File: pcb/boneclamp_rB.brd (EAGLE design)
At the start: 160 x 100 mm, 73 parts, among them IC1 24C, U1 AD8032ARZ-REEL7, U2 LT1964ES5-5TRMPBF, U4 TLV70245DBVT, U7 AD7682BCPZ, U8 TPS63700DRCT, U9 ADA4841-2YRZ

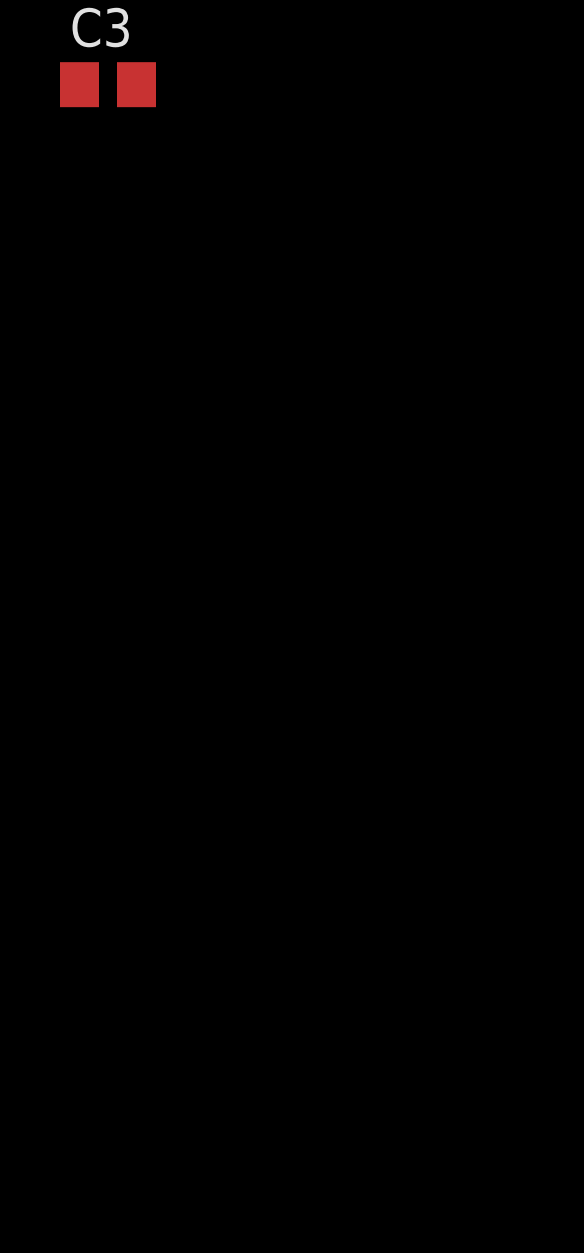
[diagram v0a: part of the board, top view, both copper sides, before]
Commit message: Properly bypassed the power and logic supplies for the DAC
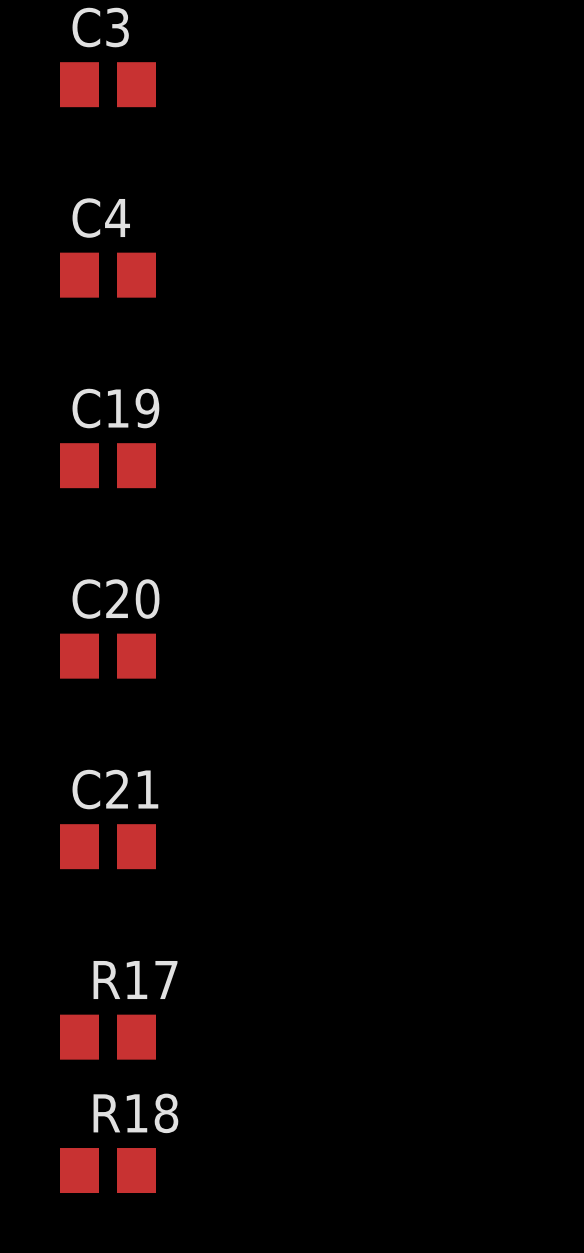
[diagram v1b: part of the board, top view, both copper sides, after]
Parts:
- added C19, C21, C4: 0.1uF, rcl:C0805
- added C20: 10uF, rcl:C0805
- added R17, R18: 10k, rcl:R0805
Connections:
- new net DAC_LDAC: R18.1, U$42.9
- new net PE: C4.2
- net AGND: now also C19.2, C20.2, C21.2; no longer U$42.9
- net DAC_RST: now also R17.1
- net VDD: now also C19.1, C20.1
- net VDRIVE: now also C4.1, R17.2, R18.2
- net VREF: now also C21.1
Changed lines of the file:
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@@
 </element>
 <element name="C3" library="rcl" package="C0805" value="10uF" x="-119.38" y="-366.395"/>
+<element name="C4" library="rcl" package="C0805" value="0.1uF" x="-119.38" y="-372.745"/>
+<element name="C19" library="rcl" package="C0805" value="0.1uF" x="-119.38" y="-379.095"/>
+<element name="C20" library="rcl" package="C0805" value="10uF" x="-119.38" y="-385.445"/>
+<element name="C21" library="rcl" package="C0805" value="0.1uF" x="-119.38" y="-391.795"/>
+<element name="R17" library="rcl" package="R0805" value="10k" x="-119.38" y="-398.145"/>
+<element name="R18" library="rcl" package="R0805" value="10k" x="-119.38" y="-402.59"/>
 </elements>
 <signals>
@@
 </polygon>
 <contactref element="C3" pad="1"/>
+<contactref element="C20" pad="1"/>
+<contactref element="C19" pad="1"/>
+<wire x1="-120.33" y1="-379.095" x2="-120.33" y2="-385.445" width="0" layer="19" extent="1-1"/>
+<wire x1="-120.33" y1="-366.395" x2="-120.33" y2="-379.095" width="0" layer="19" extent="1-1"/>
 <wire x1="-120.33" y1="-355.6" x2="-120.33" y2="-366.395" width="0" layer="19" extent="1-1"/>
 <wire x1="-108.0262" y1="-302.895" x2="-120.33" y2="-355.6" width="0" layer="19" extent="1-1"/>
@@
 <contactref element="U$42" pad="4"/>
 <contactref element="U$42" pad="10"/>
-<contactref element="U$42" pad="9"/>
 <contactref element="U$42" pad="16"/>
 <contactref element="C2" pad="2"/>
@@
 </polygon>
 <contactref element="C3" pad="2"/>
+<contactref element="C20" pad="2"/>
+<contactref element="C19" pad="2"/>
+<contactref element="C21" pad="2"/>
 <wire x1="-82.97" y1="-177.8" x2="-83.7692" y2="-167.9702" width="0" layer="19" extent="1-1"/>
 <wire x1="-82.97" y1="-184.15" x2="-82.97" y2="-177.8" width="0" layer="19" extent="1-1"/>
@@
 <wire x1="-118.43" y1="-355.6" x2="-110.91" y2="-327.66" width="0" layer="19" extent="1-1"/>
 <wire x1="-118.43" y1="-366.395" x2="-118.43" y2="-355.6" width="0" layer="19" extent="1-1"/>
+<wire x1="-118.43" y1="-379.095" x2="-118.43" y2="-366.395" width="0" layer="19" extent="1-1"/>
+<wire x1="-118.43" y1="-385.445" x2="-118.43" y2="-379.095" width="0" layer="19" extent="1-1"/>
+<wire x1="-118.43" y1="-391.795" x2="-118.43" y2="-385.445" width="0" layer="19" extent="1-1"/>
 <wire x1="-46.04" y1="-261.62" x2="-82.87" y2="-254" width="0" layer="19" extent="1-1"/>
 <wire x1="7.94" y1="48.26" x2="-59.4868" y2="-74.168" width="0" layer="19" extent="1-1"/>
@@
 <wire x1="20.5994" y1="63.246" x2="14.9606" y2="61.2902" width="0" layer="19" extent="1-1"/>
 <wire x1="20.5994" y1="59.3344" x2="20.5994" y2="63.246" width="0" layer="19" extent="1-1"/>
-<wire x1="20.5994" y1="58.674" x2="20.5994" y2="59.3344" width="0" layer="19" extent="1-1"/>
-<wire x1="25.4" y1="57.658" x2="20.5994" y2="58.674" width="0" layer="19" extent="1-1"/>
+<wire x1="25.4" y1="57.658" x2="20.5994" y2="59.3344" width="0" layer="19" extent="1-1"/>
 <wire x1="35.052" y1="59.9694" x2="25.4" y2="57.658" width="0" layer="19" extent="1-1"/>
 <wire x1="35.052" y1="60.452" x2="35.052" y2="59.9694" width="0" layer="19" extent="1-1"/>
@@
 <contactref element="U7" pad="15"/>
 <contactref element="C12" pad="1"/>
+<contactref element="C4" pad="1"/>
+<contactref element="R17" pad="2"/>
+<contactref element="R18" pad="2"/>
+<wire x1="-118.43" y1="-398.145" x2="-120.33" y2="-372.745" width="0" layer="19" extent="1-1"/>
+<wire x1="-118.43" y1="-402.59" x2="-118.43" y2="-398.145" width="0" layer="19" extent="1-1"/>
+<wire x1="-47.94" y1="-261.62" x2="-120.33" y2="-372.745" width="0" layer="19" extent="1-1"/>
+<wire x1="50.165" y1="21.59" x2="-47.94" y2="-261.62" width="0" layer="19" extent="1-1"/>
+<wire x1="52.705" y1="21.59" x2="50.165" y2="21.59" width="0" layer="19" extent="1-1"/>
+<wire x1="38.608" y1="61.9506" x2="50.165" y2="21.59" width="0" layer="19" extent="1-1"/>
+<wire x1="20.5994" y1="59.9948" x2="38.608" y2="61.9506" width="0" layer="19" extent="1-1"/>
+<wire x1="118.745" y1="21.65" x2="52.705" y2="21.59" width="0" layer="19" extent="1-1"/>
+<wire x1="138.85" y1="24.13" x2="118.745" y2="21.65" width="0" layer="19" extent="1-1"/>
 <wire x1="140.55" y1="20.32" x2="138.85" y2="24.13" width="0" layer="19" extent="1-1"/>
 <wire x1="140.55" y1="15.24" x2="140.55" y2="20.32" width="0" layer="19" extent="1-1"/>
@@
 <wire x1="140.55" y1="-5.08" x2="140.55" y2="0" width="0" layer="19" extent="1-1"/>
 <wire x1="157.48" y1="-10.16" x2="140.55" y2="-5.08" width="0" layer="19" extent="1-1"/>
-<wire x1="118.745" y1="21.65" x2="138.85" y2="24.13" width="0" layer="19" extent="1-1"/>
-<wire x1="52.705" y1="21.59" x2="118.745" y2="21.65" width="0" layer="19" extent="1-1"/>
-<wire x1="50.165" y1="21.59" x2="52.705" y2="21.59" width="0" layer="19" extent="1-1"/>
-<wire x1="38.608" y1="61.9506" x2="50.165" y2="21.59" width="0" layer="19" extent="1-1"/>
-<wire x1="20.5994" y1="59.9948" x2="38.608" y2="61.9506" width="0" layer="19" extent="1-1"/>
-<wire x1="-47.94" y1="-261.62" x2="50.165" y2="21.59" width="0" layer="19" extent="1-1"/>
 </signal>
 <signal name="VDD_5V">
@@
 <contactref element="R15" pad="1"/>
 <contactref element="U$42" pad="1"/>
+<contactref element="C21" pad="1"/>
 <wire x1="-112.9538" y1="-304.165" x2="-112.61" y2="-321.31" width="0" layer="19" extent="1-1"/>
 <wire x1="-112.9538" y1="-302.895" x2="-112.9538" y2="-304.165" width="0" layer="19" extent="1-1"/>
+<wire x1="-120.33" y1="-391.795" x2="-112.61" y2="-321.31" width="0" layer="19" extent="1-1"/>
 <wire x1="14.9606" y1="63.246" x2="-112.9538" y2="-302.895" width="0" layer="19" extent="1-1"/>
 </signal>
@@
 <signal name="DAC_RST">
 <contactref element="U$42" pad="15"/>
+<contactref element="R17" pad="1"/>
+<wire x1="-120.33" y1="-398.145" x2="20.5994" y2="62.5856" width="0" layer="19" extent="1-1"/>
 </signal>
 <signal name="DAC_CS">
@@
 <contactref element="U$1" pad="102"/>
 </signal>
+<signal name="PE">
+<contactref element="C4" pad="2"/>
+</signal>
+<signal name="DAC_LDAC">
+<contactref element="R18" pad="1"/>
+<contactref element="U$42" pad="9"/>
+<wire x1="-120.33" y1="-402.59" x2="20.5994" y2="58.674" width="0" layer="19" extent="1-1"/>
+</signal>
 </signals>

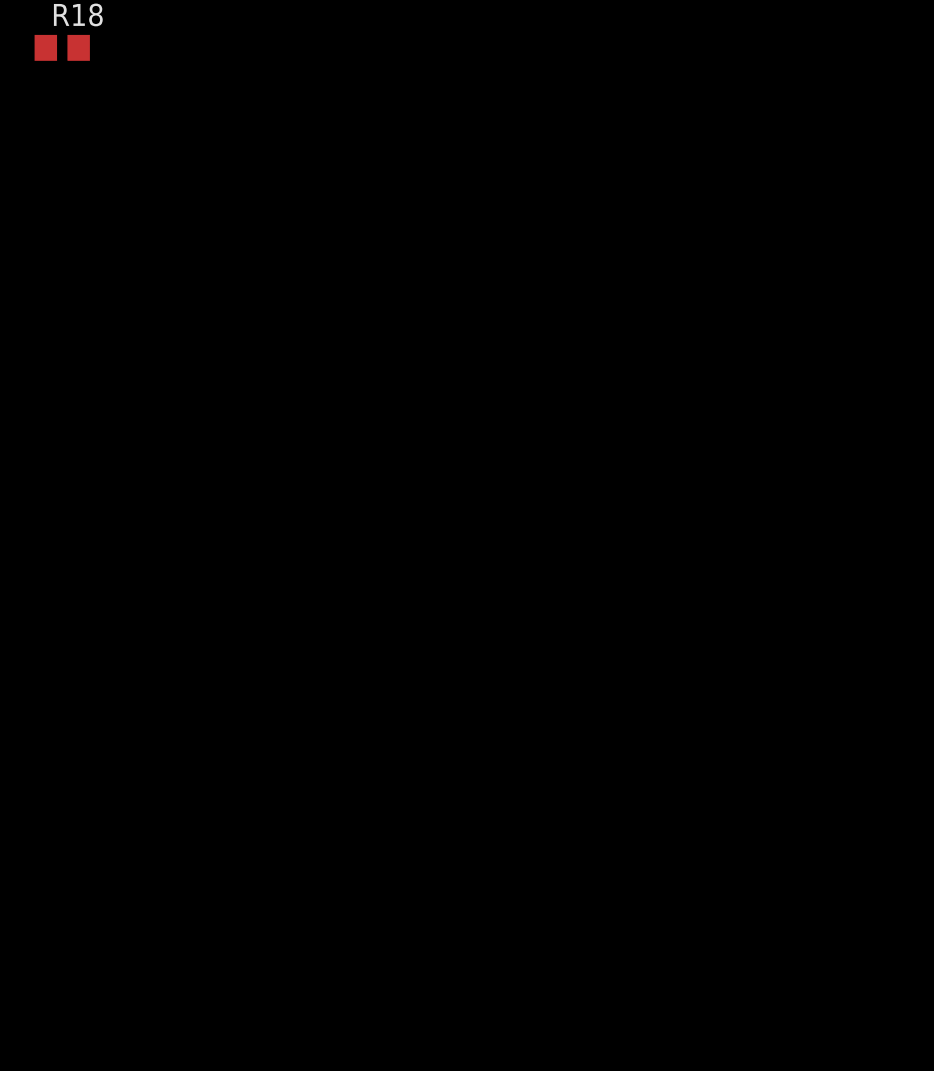
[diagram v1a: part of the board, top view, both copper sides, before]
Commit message: Added Stefano's biasing circuitry back into the master branch schematic. Automatic merge was not going to work properly
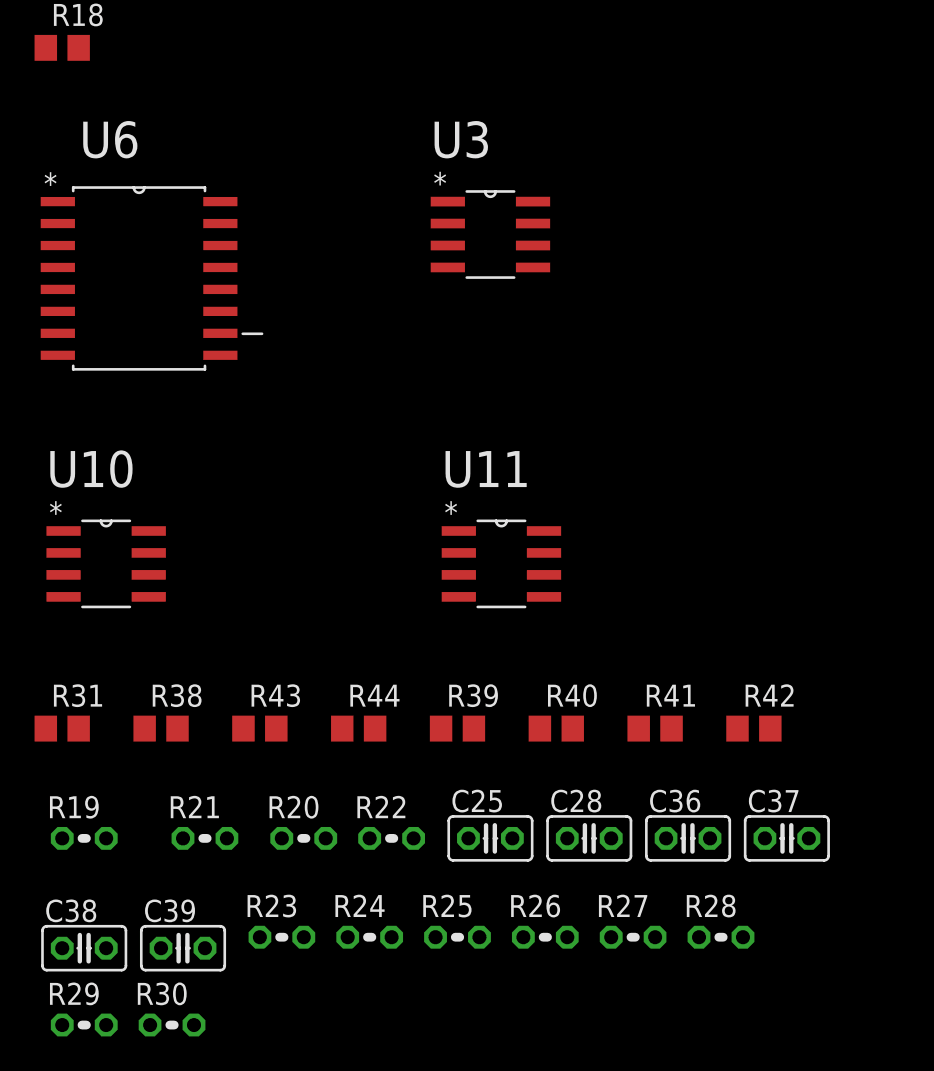
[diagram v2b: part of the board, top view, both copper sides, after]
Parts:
- added C25, C28, C36, C37, C38, C39: (no value), resistor:C025-025X050
- added R19: 6.937k, resistor:0204V
- added R20, R22: 10k, resistor:0204V
- added R21: 6.66k, resistor:0204V
- added R23, R24, R25, R26, R27, R28, R29, R30: (no value), resistor:0204V
- added R31, R38, R43, R44: 0.1k, rcl:R0805
- added R39, R40, R41, R42: 10k, rcl:R0805
- added U10, U11, U3: ADA4841-2YRZ, analog-devices-01:SOIC127P600X175-8N
- added U6: AD713JRZ-16, analog-devices-01:SOIC127P1032X265-16N
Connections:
- new net N$3: R26.2, R30.1, U6.14
- new net N$52: R25.2, R29.1, U6.12
- new net N$53: C38.2, R21.1, R22.2, U3.5
- new net N$54: C28.2, R19.1, R20.2, U3.3
- new net N$55: R24.2, R28.1, U6.5
- new net N$56: R23.2, R27.1, U6.3
- new net N$57: C25.2, R20.1
- new net N$58: C37.1
- new net N$59: R22.1
- new net VBIAS_DOWN: C39.2, U3.6, U3.7, U6.11, U6.15, U6.2, U6.6
- new net VBIAS_UP: C36.2, R31.2, R38.2, R39.1, R39.2, R40.1, R40.2, R41.1, R41.2, R42.1, R42.2, R43.2, R44.2, U10.2, U10.6, U11.2, U11.6, U3.1, U3.2
- net ADC_A: now also U10.3
- net ADC_B: now also U10.5
- net ADC_C: now also U11.3
- net ADC_D: now also U11.5
- net GND: now also C25.1, C28.1, C36.1, C38.1, C39.1, U6.8, U6.9
- net VDD: now also R19.2, U10.8, U11.8, U3.8, U6.4
- net VSS: now also R21.2, U10.4, U11.4, U3.4, U6.13
- net _ADC_A: now also R38.1, U10.1
- net _ADC_B: now also R31.1, U10.7
- net _ADC_C: now also R43.1, U11.1
- net _ADC_D: now also R44.1, U11.7
- net _DAC_A: now also R23.1, R30.2, U6.16
- net _DAC_B: now also R26.1, R27.2, U6.1
- net _DAC_C: now also R25.1, R28.2, U6.7
- net _DAC_D: now also R24.1, R29.2, U6.10

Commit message: Fixed the input biasing scheme. The op-amps we are using require -0.25 to 5.2 volt supply range to push the inputs into the 0 to 4.096 range required by the ADC. This means that our positive rail is too low. We need a boost conveter for the positive rail before the LDO.
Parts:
- added C40, C41, C46, C47, C48, C49, C50, C55, C56: 0.1uF, rcl:C0805
- added C42, C43, C51, C52: 2.7nF, rcl:C0805
- added C44, C45, C53, C54: 10uF, rcl:C0805
- added R32, R33, R36, R37: 33, rcl:R0603
- added R34, R35, R45, R46: 590, rcl:R0603
- added U5: ADA4841-2YRZ, analog-devices-01:SOIC127P600X175-8N
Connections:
- removed net +VS: U9.8
- removed net -VS: U9.4
- removed net SGND: JP5.1, JP5.2
- new net ADC_COM: JP5.2
- new net DAC_COM: JP5.1
- new net N$1: R37.2, R45.1, U5.6, U5.7
- new net N$2: R33.2, R34.1, U9.6, U9.7
- new net N$20: R32.2, R35.1, U9.1, U9.2
- new net N$5: R36.2, R46.1, U5.1, U5.2
- new net VBIAS: C46.1, C47.1, C48.1, C55.1, C56.1, R34.2, R35.2, R45.2, R46.2, U1.6, U1.7
- net ADC_A: now also U9.3
- net ADC_B: now also U9.5
- net ADC_C: now also U5.3
- net ADC_D: now also U5.5
- net AGND: now also C40.2, C41.2, C42.2, C43.2, C44.1, C45.2, C46.2, C47.2, C48.2, C49.2, C50.2, C51.2, C52.2, C53.1, C54.2, C55.2, C56.2
- net VCOM: no longer U1.6, U1.7
- net VDD: now also C40.1, C45.1, C49.1, C54.1, U5.8, U9.8
- net VSS: now also C41.1, C44.2, C50.1, C53.2, U5.4, U9.4
- net _ADC_A: now also C42.1, R32.1
- net _ADC_B: now also C43.1, R33.1
- net _ADC_C: now also C51.1, R36.1
- net _ADC_D: now also C52.1, R37.1

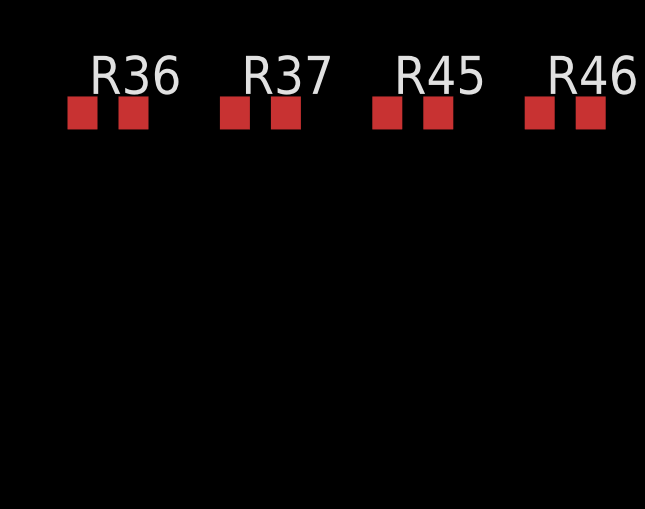
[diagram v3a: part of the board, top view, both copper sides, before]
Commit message: I found a potentially better option for the ADC. It is a 100KSPS Serial sampling device from TI. It accepts true bipolar signals of +-VREF using a single supply. It also has as a more resonable SMD package.
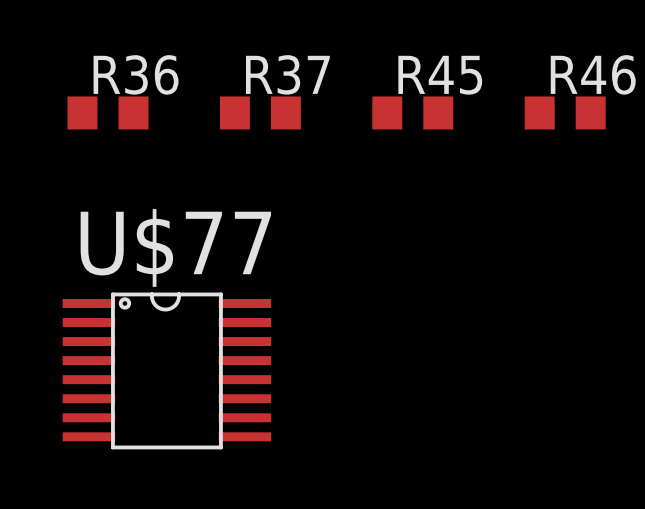
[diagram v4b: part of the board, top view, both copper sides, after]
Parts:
- added U$77: ADS8343, ti-extended:SOP63P500X150-16N
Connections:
- new net VCC: U$77.1, U$77.9
- net GND: now also U$77.10, U$77.11
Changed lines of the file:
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@@
 <element name="C55" library="rcl" package="C0805" value="0.1uF" x="-119.38" y="-561.34"/>
 <element name="C56" library="rcl" package="C0805" value="0.1uF" x="-113.03" y="-561.34"/>
+<element name="U$77" library="ti-extended" package="SOP63P500X150-16N" value="ADS8343" x="-120.015" y="-573.405"/>
 </elements>
 <signals>
@@
 <contactref element="U6" pad="8"/>
 <contactref element="U6" pad="9"/>
-<wire x1="52.705" y1="72.39" x2="52.705" y2="74.93" width="0" layer="19" extent="1-1"/>
-<wire x1="52.705" y1="19.05" x2="52.705" y2="72.39" width="0" layer="19" extent="1-1"/>
-<wire x1="50.165" y1="19.05" x2="52.705" y2="19.05" width="0" layer="19" extent="1-1"/>
-<wire x1="4.445" y1="19.05" x2="50.165" y2="19.05" width="0" layer="19" extent="1-1"/>
-<wire x1="1.905" y1="19.05" x2="4.445" y2="19.05" width="0" layer="19" extent="1-1"/>
-<wire x1="-110.236" y1="-420.37" x2="1.905" y2="19.05" width="0" layer="19" extent="1-1"/>
-<wire x1="-119.634" y1="-420.37" x2="-110.236" y2="-420.37" width="0" layer="19" extent="1-1"/>
-<wire x1="-95.885" y1="-448.31" x2="-110.236" y2="-420.37" width="0" layer="19" extent="1-1"/>
+<contactref element="U$77" pad="11"/>
+<contactref element="U$77" pad="10"/>
+<wire x1="-114.815" y1="-577.215" x2="-114.815" y2="-576.58" width="0" layer="19" extent="1-1"/>
+<wire x1="-113.665" y1="-454.66" x2="-114.815" y2="-576.58" width="0" layer="19" extent="1-1"/>
+<wire x1="-119.38" y1="-454.66" x2="-113.665" y2="-454.66" width="0" layer="19" extent="1-1"/>
+<wire x1="-95.885" y1="-448.31" x2="-113.665" y2="-454.66" width="0" layer="19" extent="1-1"/>
 <wire x1="-90.17" y1="-448.31" x2="-95.885" y2="-448.31" width="0" layer="19" extent="1-1"/>
 <wire x1="-84.455" y1="-448.31" x2="-90.17" y2="-448.31" width="0" layer="19" extent="1-1"/>
-<wire x1="-113.665" y1="-454.66" x2="-95.885" y2="-448.31" width="0" layer="19" extent="1-1"/>
-<wire x1="-119.38" y1="-454.66" x2="-113.665" y2="-454.66" width="0" layer="19" extent="1-1"/>
+<wire x1="-110.236" y1="-420.37" x2="-95.885" y2="-448.31" width="0" layer="19" extent="1-1"/>
+<wire x1="-119.634" y1="-420.37" x2="-110.236" y2="-420.37" width="0" layer="19" extent="1-1"/>
+<wire x1="1.905" y1="19.05" x2="-110.236" y2="-420.37" width="0" layer="19" extent="1-1"/>
+<wire x1="4.445" y1="19.05" x2="1.905" y2="19.05" width="0" layer="19" extent="1-1"/>
+<wire x1="50.165" y1="19.05" x2="4.445" y2="19.05" width="0" layer="19" extent="1-1"/>
+<wire x1="52.705" y1="19.05" x2="50.165" y2="19.05" width="0" layer="19" extent="1-1"/>
+<wire x1="52.705" y1="72.39" x2="52.705" y2="19.05" width="0" layer="19" extent="1-1"/>
+<wire x1="52.705" y1="74.93" x2="52.705" y2="72.39" width="0" layer="19" extent="1-1"/>
 </signal>
 <signal name="BAT_SENSE">
@@
 <wire x1="-119.3038" y1="-543.56" x2="-119.3038" y2="-544.83" width="0" layer="19" extent="1-1"/>
 </signal>
+<signal name="VCC">
+<contactref element="U$77" pad="9"/>
+<contactref element="U$77" pad="1"/>
+<wire x1="-120.015" y1="-573.405" x2="-114.815" y2="-577.85" width="0" layer="19" extent="1-1"/>
+</signal>
 </signals>
